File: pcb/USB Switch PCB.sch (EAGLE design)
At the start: 31 parts, among them Q1 2N7002P, Q2 2N7002P, X2 UE27-USBA

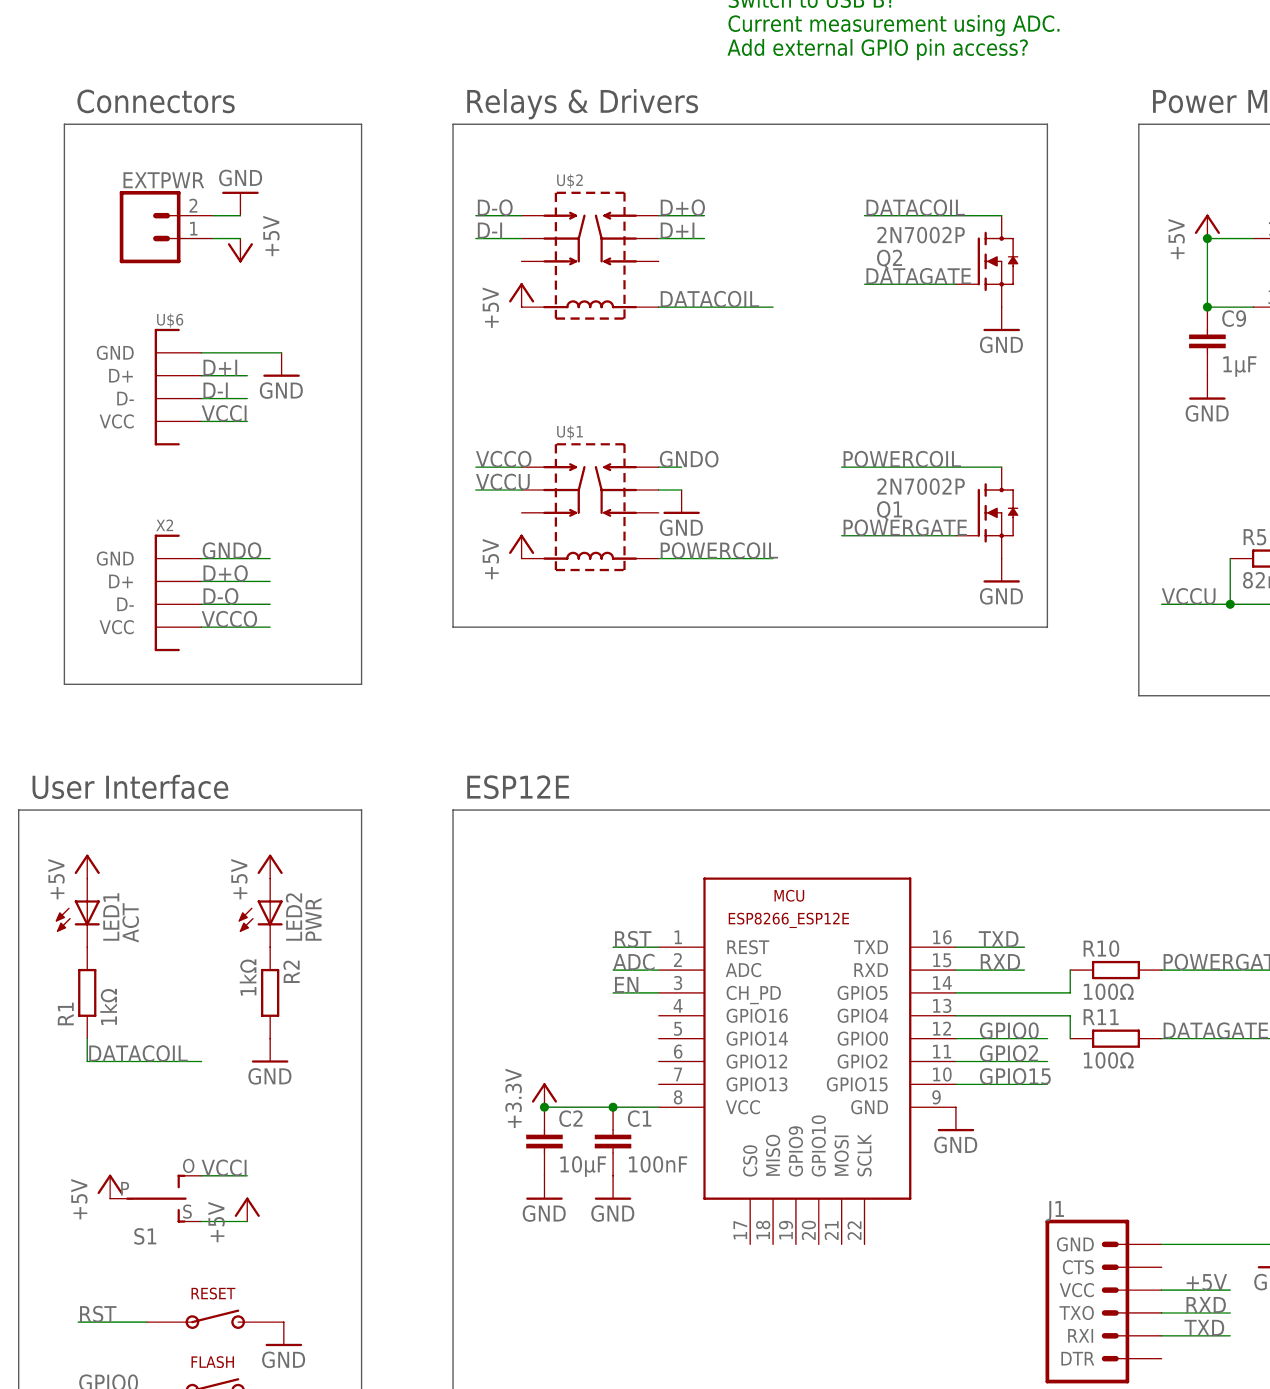
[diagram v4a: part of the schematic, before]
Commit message: Remade PCB layout.
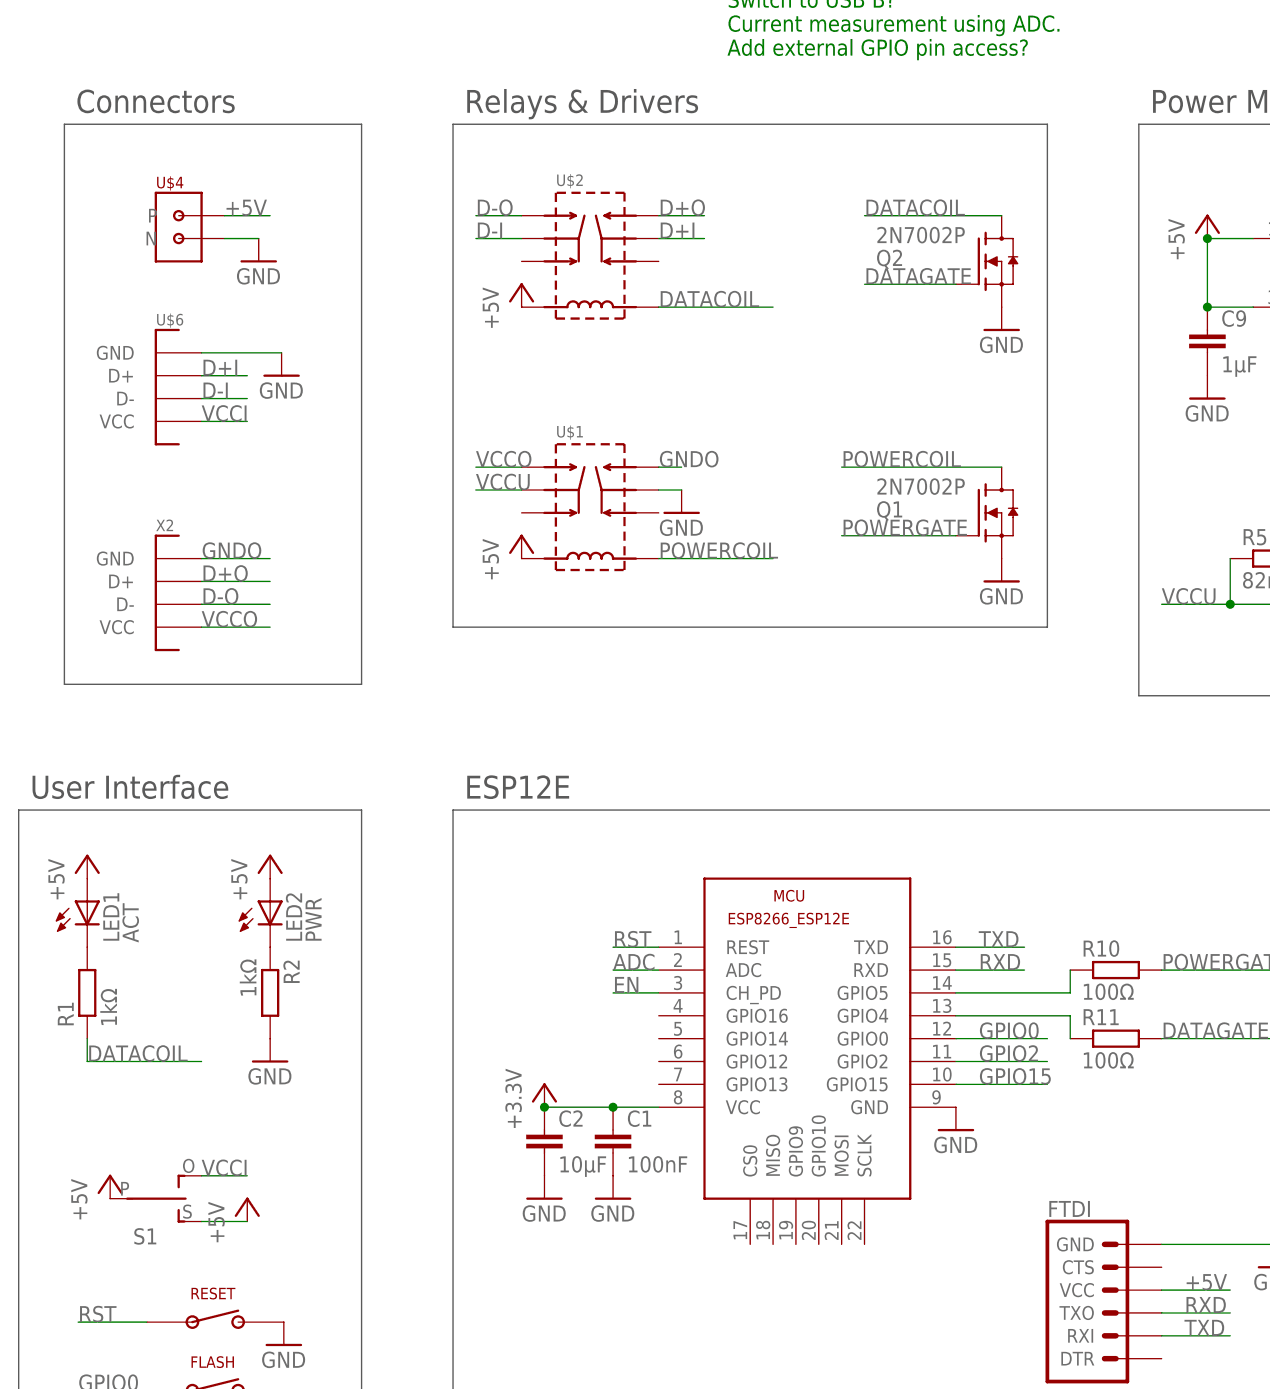
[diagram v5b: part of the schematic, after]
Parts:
- removed EXTPWR: (no value), SparkFun-Connectors:CONN_02
- added U$4: TERMINAL-BLOCK, USB Switch PCB:TERMINAL-BLOCK
- renumbered J1 to FTDI
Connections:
- net +5V: now also U$4.P; no longer EXTPWR.1
- net GND: now also U$4.N; no longer EXTPWR.2
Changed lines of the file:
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@@
 <part name="X2" library="USB Switch PCB" deviceset="UE27-USBA" device=""/>
 <part name="P+4" library="supply1" library_urn="urn:adsk.eagle:library:371" deviceset="+5V" device=""/>
-<part name="EXTPWR" library="SparkFun-Connectors" deviceset="CONN_02" device=""/>
-<part name="GND7" library="supply1" library_urn="urn:adsk.eagle:library:371" deviceset="GND" device=""/>
-<part name="P+7" library="supply1" library_urn="urn:adsk.eagle:library:371" deviceset="+5V" device=""/>
 <part name="MCU" library="ESP8266-ESP12E" deviceset="ESP8266-12E" device="ESP8266-ESP12E"/>
 <part name="3V3" library="supply1" library_urn="urn:adsk.eagle:library:371" deviceset="+5V" device="" value="+3.3V"/>
@@
 <part name="R11" library="rcl" library_urn="urn:adsk.eagle:library:334" deviceset="R-EU_" device="R0603" package3d_urn="urn:adsk.eagle:package:23555/2" value="100Ω"/>
 <part name="U$6" library="USB Switch PCB" deviceset="USB-B" device=""/>
-<part name="J1" library="SparkFun-Connectors" deviceset="6_PIN_SERIAL_TARGET" device=""/>
+<part name="FTDI" library="SparkFun-Connectors" deviceset="6_PIN_SERIAL_TARGET" device=""/>
 <part name="GND8" library="supply1" library_urn="urn:adsk.eagle:library:371" deviceset="GND" device=""/>
 <part name="RESET" library="USB Switch PCB" deviceset="MOMENTARY-SWITCH" device=""/>
@@
 <part name="3V1" library="supply1" library_urn="urn:adsk.eagle:library:371" deviceset="+5V" device="" value="+3.3V"/>
 <part name="GND14" library="supply1" library_urn="urn:adsk.eagle:library:371" deviceset="GND" device=""/>
+<part name="U$4" library="USB Switch PCB" deviceset="TERMINAL-BLOCK" device=""/>
+<part name="GND2" library="supply1" library_urn="urn:adsk.eagle:library:371" deviceset="GND" device=""/>
 </parts>
 <sheets>
@@
 <instance part="X2" gate="G$1" x="-78.74" y="76.2"/>
 <instance part="P+4" gate="1" x="-71.12" y="12.7"/>
-<instance part="EXTPWR" gate="G$1" x="-82.55" y="119.38"/>
-<instance part="GND7" gate="1" x="-71.882" y="124.46" rot="R180"/>
-<instance part="P+7" gate="1" x="-71.882" y="116.84" rot="R180"/>
 <instance part="MCU" gate="G$1" x="-2.54" y="33.02"/>
 <instance part="3V3" gate="1" x="-38.1" y="25.4"/>
@@
 <instance part="R11" gate="G$1" x="25.4" y="30.48"/>
 <instance part="U$6" gate="G$1" x="-78.74" y="99.06"/>
-<instance part="J1" gate="G$1" x="25.4" y="0"/>
+<instance part="FTDI" gate="G$1" x="25.4" y="0"/>
 <instance part="GND8" gate="1" x="43.18" y="5.08"/>
 <instance part="RESET" gate="G$1" x="-74.676" y="-1.016"/>
@@
 <instance part="3V1" gate="1" x="78.74" y="83.82"/>
 <instance part="GND14" gate="1" x="68.58" y="73.66"/>
+<instance part="U$4" gate="G$1" x="-78.74" y="121.92"/>
+<instance part="GND2" gate="1" x="-69.85" y="116.84"/>
 </instances>
 <busses>
@@
 </segment>
 <segment>
-<pinref part="EXTPWR" gate="G$1" pin="2"/>
-<pinref part="GND7" gate="1" pin="GND"/>
-<wire x1="-74.93" y1="121.92" x2="-71.882" y2="121.92" width="0.1524" layer="91"/>
-</segment>
-<segment>
 <pinref part="C2" gate="G$1" pin="2"/>
 <pinref part="GND9" gate="1" pin="GND"/>
@@
 </segment>
 <segment>
-<pinref part="J1" gate="G$1" pin="GND"/>
+<pinref part="FTDI" gate="G$1" pin="GND"/>
 <pinref part="GND8" gate="1" pin="GND"/>
 <wire x1="30.48" y1="7.62" x2="43.18" y2="7.62" width="0.1524" layer="91"/>
@@
 <pinref part="U$3" gate="G$1" pin="GND"/>
 <pinref part="GND14" gate="1" pin="GND"/>
+</segment>
+<segment>
+<pinref part="U$4" gate="G$1" pin="N"/>
+<wire x1="-73.66" y1="119.38" x2="-69.85" y2="119.38" width="0.1524" layer="91"/>
+<pinref part="GND2" gate="1" pin="GND"/>
 </segment>
 </net>
@@
 <wire x1="-76.2" y1="10.16" x2="-71.12" y2="10.16" width="0.1524" layer="91"/>
 <pinref part="P+4" gate="1" pin="+5V"/>
-</segment>
-<segment>
-<pinref part="EXTPWR" gate="G$1" pin="1"/>
-<pinref part="P+7" gate="1" pin="+5V"/>
-<wire x1="-74.93" y1="119.38" x2="-71.882" y2="119.38" width="0.1524" layer="91"/>
 </segment>
 <segment>
@@
 </segment>
 <segment>
-<pinref part="J1" gate="G$1" pin="VCC"/>
+<pinref part="FTDI" gate="G$1" pin="VCC"/>
 <wire x1="30.48" y1="2.54" x2="38.1" y2="2.54" width="0.1524" layer="91"/>
 <label x="33.02" y="2.54" size="1.778" layer="95"/>
@@
 <pinref part="3V1" gate="1" pin="+5V"/>
 <wire x1="68.58" y1="81.28" x2="78.74" y2="81.28" width="0.1524" layer="91"/>
+</segment>
+<segment>
+<pinref part="U$4" gate="G$1" pin="P"/>
+<wire x1="-73.66" y1="121.92" x2="-68.58" y2="121.92" width="0.1524" layer="91"/>
+<label x="-73.66" y="121.92" size="1.778" layer="95"/>
 </segment>
 </net>
@@
 </segment>
 <segment>
-<pinref part="J1" gate="G$1" pin="RXI"/>
+<pinref part="FTDI" gate="G$1" pin="RXI"/>
 <wire x1="30.48" y1="-2.54" x2="38.1" y2="-2.54" width="0.1524" layer="91"/>
 <label x="33.02" y="-2.54" size="1.778" layer="95"/>
@@
 </segment>
 <segment>
-<pinref part="J1" gate="G$1" pin="TXO"/>
+<pinref part="FTDI" gate="G$1" pin="TXO"/>
 <wire x1="30.48" y1="0" x2="38.1" y2="0" width="0.1524" layer="91"/>
 <label x="33.02" y="0" size="1.778" layer="95"/>

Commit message: Is this final? It sure feels like final!
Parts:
- added DISP: (no value), SparkFun-Connectors:CONN_04
- renumbered U$1 to PWR, U$2 to DAT, U$3 to MEAS, U$4 to EXTPWR, U$5 to REG, U$6 to USBIN, X2 to USBOUT
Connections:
- new net SCK: DISP.3, MCU.SCLK
- new net SDA: DISP.4, MCU.MOSI
- net +5V: now also DISP.2; no longer S1.S
- net GND: now also DISP.1
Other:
- note removed: "TODO: Switch to USB B? Current measurement using ADC. Add external GPIO pin access?"
